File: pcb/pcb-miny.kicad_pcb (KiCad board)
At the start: 2 copper layers, 139.8 x 99.8 mm, 110 parts, among them SW1 Switch, SW10 Switch, SW11 Switch, SW12 Switch, SW13 Switch, SW14 Switch, SW15 Switch, SW16 Switch, SW17 Switch, SW18 Switch, SW19 Switch, SW2 Switch, SW20 Switch, SW21 Switch, SW22 Switch, SW23 Switch, SW24 Switch, SW25 Switch, SW26 Switch, SW27 Switch, SW28 Switch, SW29 Switch, SW3 Switch, SW30 Switch, SW31 Switch, SW32 Switch, SW33 Switch, SW34 Switch, SW4 Switch, SW5 Switch, SW6 Switch, SW7 Switch, SW8 Switch, SW9 Switch

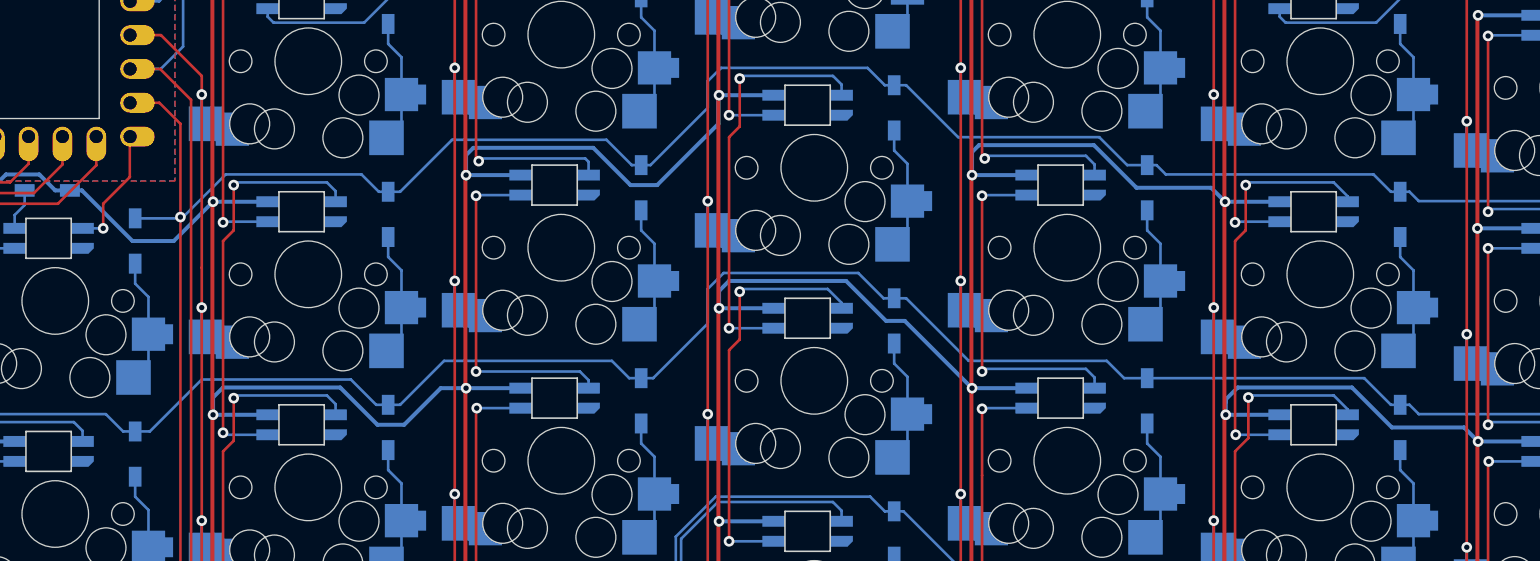
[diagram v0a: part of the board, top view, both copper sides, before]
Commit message: add decoupling capacitors
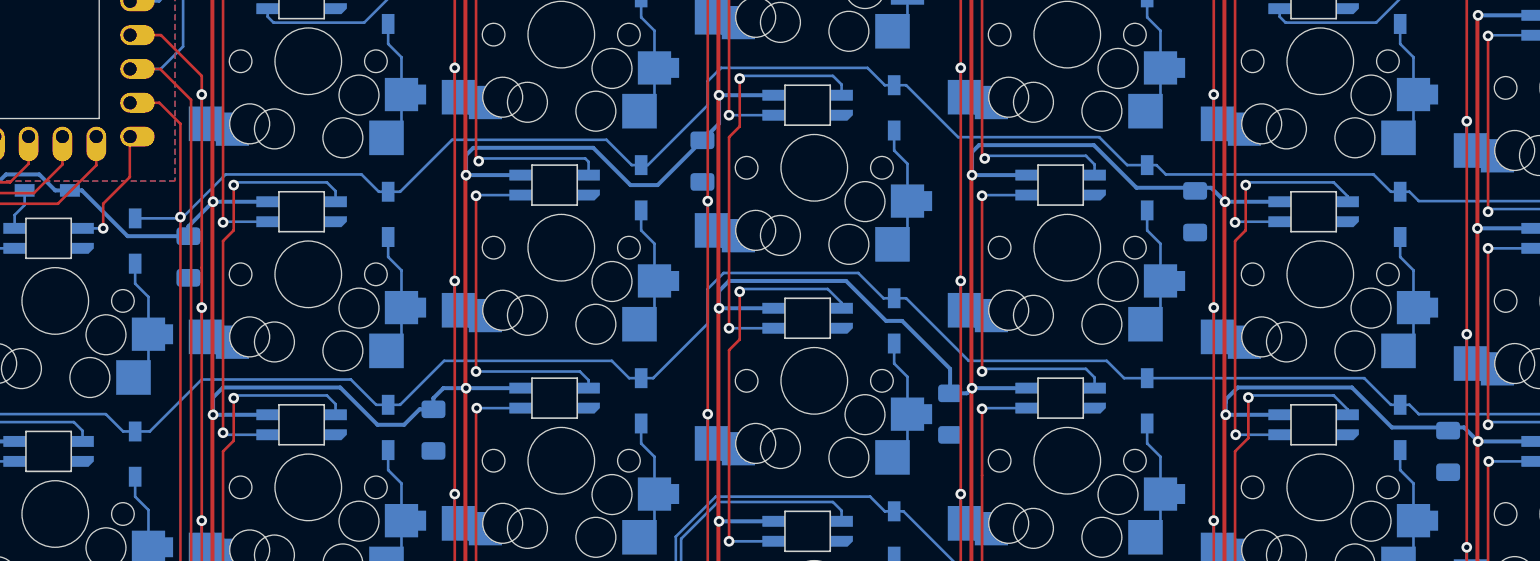
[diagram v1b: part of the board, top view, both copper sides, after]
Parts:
- added C1: 100n, Capacitor_SMD:C_1206_3216Metric_Pad1.33x1.80mm_HandSolder, B.Cu at (40.5, 101.7)
- added C2: 100n, Capacitor_SMD:C_1206_3216Metric_Pad1.33x1.80mm_HandSolder, B.Cu at (58.9, 114.7)
- added C3: 100n, Capacitor_SMD:C_1206_3216Metric_Pad1.33x1.80mm_HandSolder, B.Cu at (79.1, 94.5)
- added C4: 100n, Capacitor_SMD:C_1206_3216Metric_Pad1.33x1.80mm_HandSolder, B.Cu at (97.7, 113.5)
- added C5: 100n, Capacitor_SMD:C_1206_3216Metric_Pad1.33x1.80mm_HandSolder, B.Cu at (116.1, 98.3)
- added C6: 100n, Capacitor_SMD:C_1206_3216Metric_Pad1.33x1.80mm_HandSolder, B.Cu at (135.1, 116.3)
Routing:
- net +5V: track 712.8 -> 714.9 mm
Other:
- board text added: "JLCJLCJLCJLC"
